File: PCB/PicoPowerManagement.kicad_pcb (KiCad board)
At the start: 4 copper layers, 138.7 x 119.1 mm, 113 parts, among them J1 UART Header, J10 GSB3CA11310DSHR, J11 GSB3CA11310DSHR, J12 GSB3CA11310DSHR, J13 GSB3CA11310DSHR, J2 DEBUG, J3 SwitchLEDS, J4 PowerSwitch, J5 NAS Fan 1, J6 NAS Fan 2, J7 ATX 24P Connection, J8 GSB3CA11310DSHR, J9 GSB3CA11310DSHR, Q1 2N3904, Q10 PMOS, Q11 PMOS, Q12 PMOS, Q13 PMOS, Q2 PMOS, Q3 PMOS, Q4 PMOS, Q5 PMOS, Q6 PMOS, Q7 PMOS, Q8 PMOS, Q9 PMOS, U10 FUSB302B10MPX, U11 FUSB302B11MPX, U12 LM338T/NOPB, U13 LM338T/NOPB, U14 LM338T/NOPB, U18 LM338T/NOPB, U19 LM338T/NOPB, U2 LP5810ADSDR, U20 LM338T/NOPB, U3 LP5810ADSDR, U4 LSF0101DRYR, U5 LSF0101DRYR, U6 FUSB002B01MPX, U7 FUSB002B10MPX, U8 FUSB002B11MPX, U9 FUSB302B01MPX

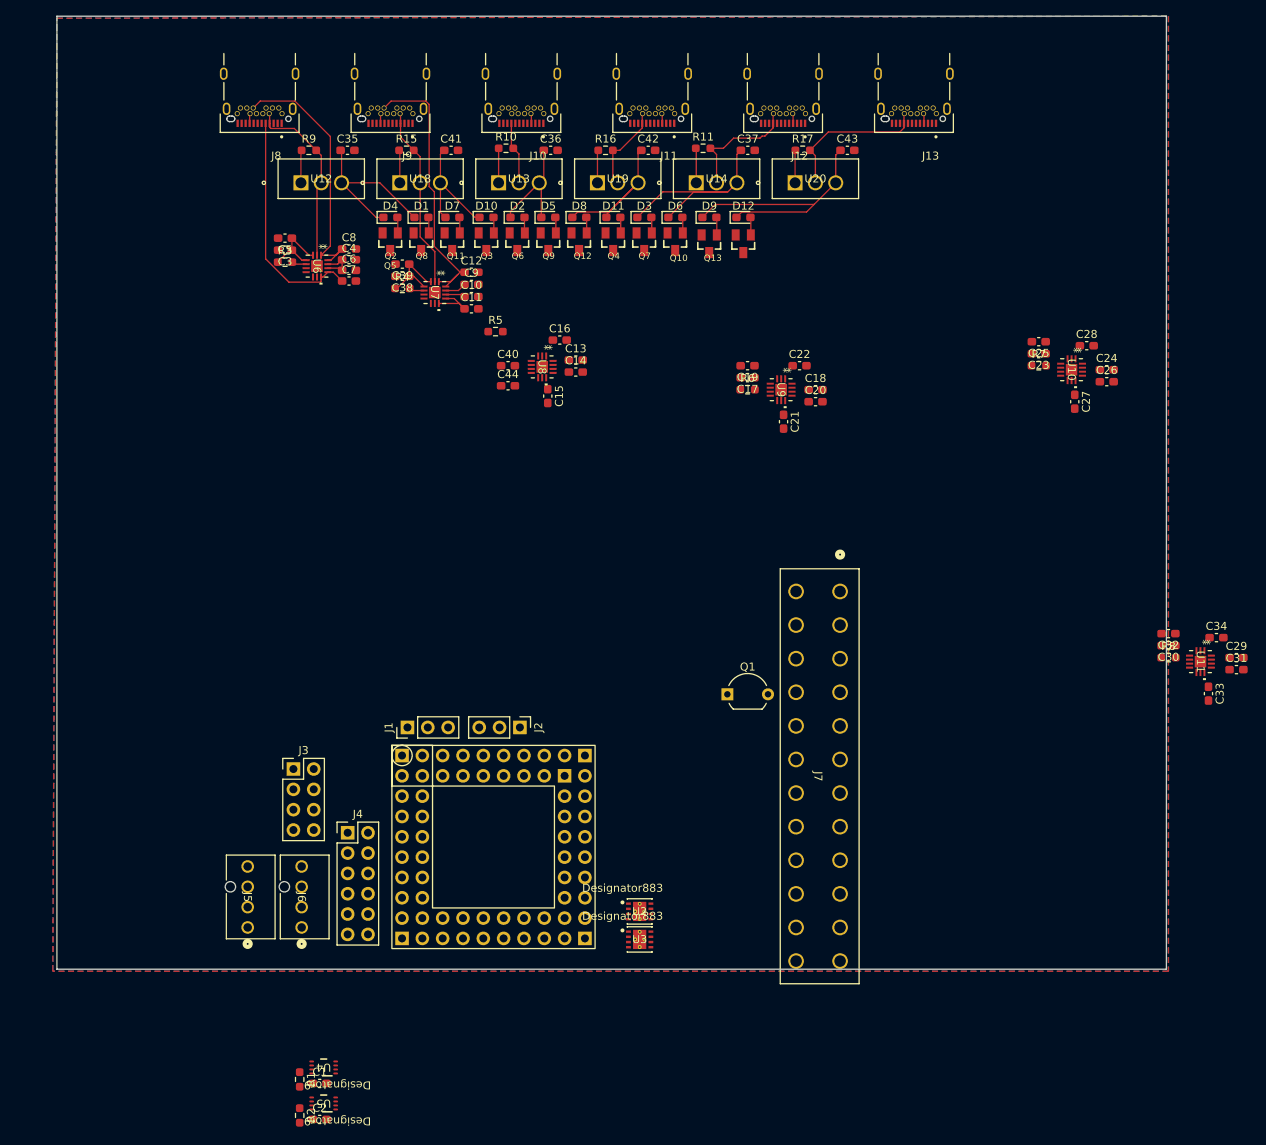
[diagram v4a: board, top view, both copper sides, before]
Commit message: Add 2N3904 component library and update footprint and symbol definitions
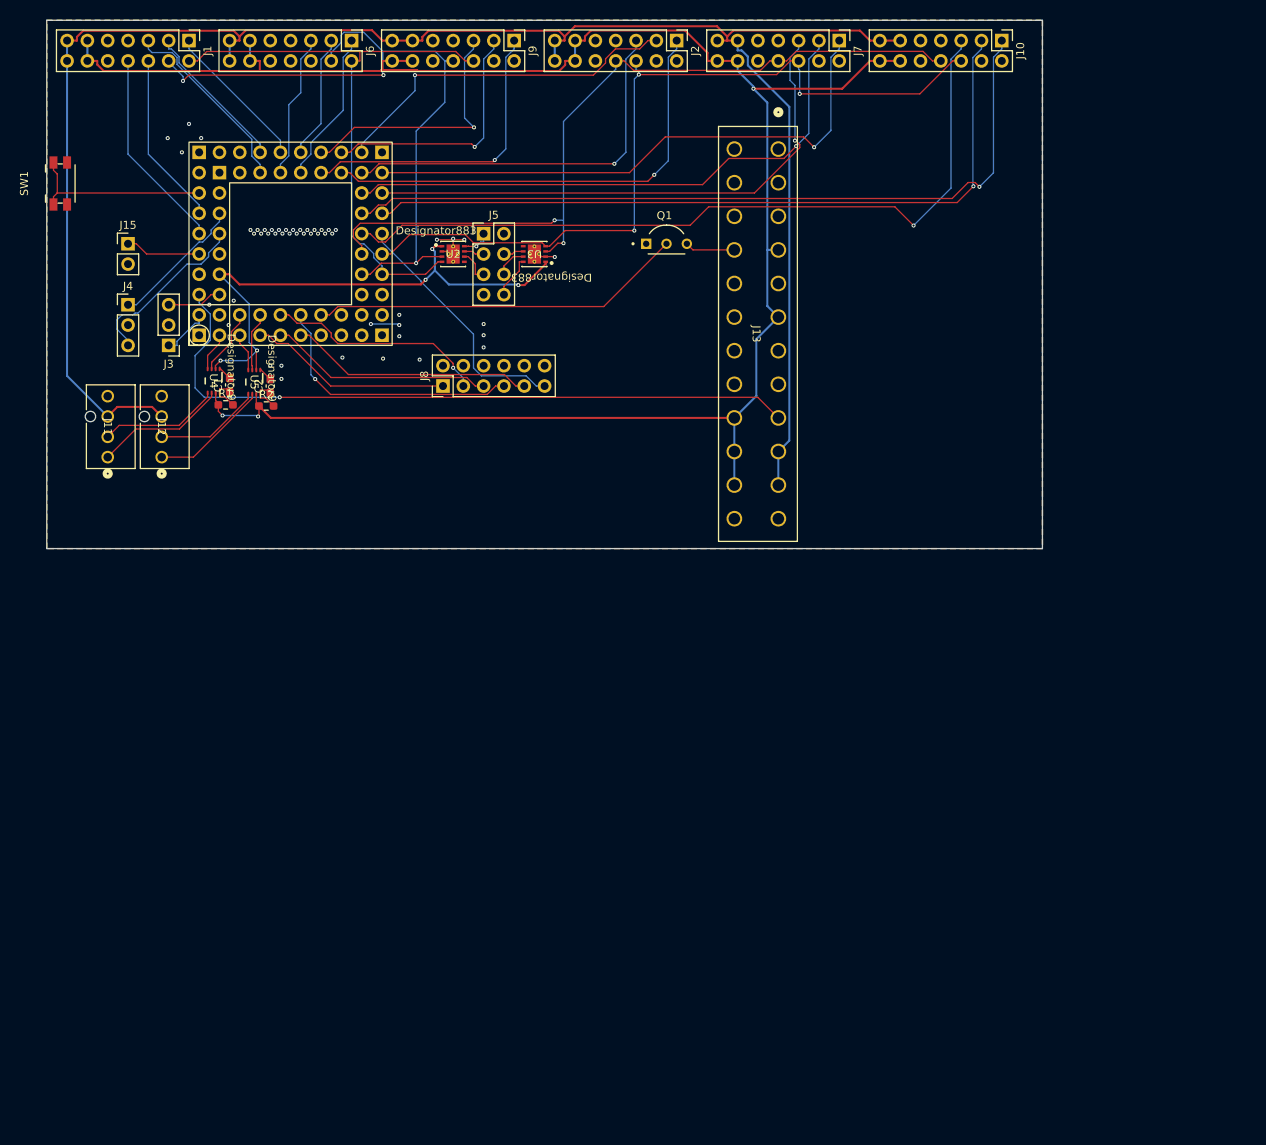
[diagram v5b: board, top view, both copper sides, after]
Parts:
- removed C10, C14, C17, C20, C23, C26, C29, C3, C32, C35, C36, C37, C38, C40, C41, C42, C43, C6: 0.1uF, Capacitor_SMD:C_0603_1608Metric_Pad1.08x0.95mm_HandSolder
- removed C11, C12, C15, C16, C21, C22, C27, C28, C33, C34, C7, C8: 200pF, Capacitor_SMD:C_0603_1608Metric_Pad1.08x0.95mm_HandSolder
- removed C13, C18, C24, C30, C4, C9: 10uF, Capacitor_SMD:C_0603_1608Metric_Pad1.08x0.95mm_HandSolder
- removed C19, C25, C31, C39, C44, C5: 1uF, Capacitor_SMD:C_0603_1608Metric_Pad1.08x0.95mm_HandSolder
- removed D1, D10, D11, D12, D2, D3, D4, D5, D6, D7, D8, D9: D_Small, Diode_SMD:D_0603_1608Metric_Pad1.05x0.95mm_HandSolder
- removed the J11 at (101.1, 32.6)
- removed the J12 at (117.4, 32.6)
- removed the J13 at (133.8, 32.6)
- removed the J8 at (52.0, 32.6)
- removed Q10, Q11, Q12, Q13, Q2, Q3, Q4, Q5, Q6, Q7, Q8, Q9: PMOS, SI2312:SOT23
- removed R10, R11, R15, R16, R17, R9: 0.25, Resistor_SMD:R_0603_1608Metric_Pad0.98x0.95mm_HandSolder
- removed R3, R4, R5, R6, R7, R8: 4.7k, Resistor_SMD:R_0603_1608Metric_Pad0.98x0.95mm_HandSolder
- removed U10: FUSB302B10MPX, FUSB302:MLP14_2P5X2P5_ONS
- removed U11: FUSB302B11MPX, FUSB302:MLP14_2P5X2P5_ONS
- removed U12, U13, U14, U18, U19, U20: LM338T/NOPB, LM338:T03B_TEX
- removed U6: FUSB002B01MPX, FUSB302:MLP14_2P5X2P5_ONS
- removed U7: FUSB002B10MPX, FUSB302:MLP14_2P5X2P5_ONS
- removed U8: FUSB002B11MPX, FUSB302:MLP14_2P5X2P5_ONS
- removed U9: FUSB302B01MPX, FUSB302:MLP14_2P5X2P5_ONS
- added J1: Conn_02x07_Odd_Even, Connector_PinHeader_2.54mm:PinHeader_2x07_P2.54mm_Vertical, F.Cu at (43.2, 22.9)
- added J15: Conn_01x02, Connector_PinHeader_2.54mm:PinHeader_1x02_P2.54mm_Vertical, F.Cu at (35.6, 48.3)
- added J2: Conn_02x07_Odd_Even, Connector_PinHeader_2.54mm:PinHeader_2x07_P2.54mm_Vertical, F.Cu at (104.1, 22.9)
- added J6: Conn_02x07_Odd_Even, Connector_PinHeader_2.54mm:PinHeader_2x07_P2.54mm_Vertical, F.Cu at (63.5, 22.9)
- added J7: Conn_02x07_Odd_Even, Connector_PinHeader_2.54mm:PinHeader_2x07_P2.54mm_Vertical, F.Cu at (124.5, 22.9)
- added SW1: SW_SPST, Button_Switch_SMD:Panasonic_EVQPUJ_EVQPUA, F.Cu at (27.1, 40.7)
- J10, J9: value GSB3CA11310DSHR -> Conn_02x07_Odd_Even; footprint GSB3CA11310DSHR:AMPHENOL_GSB3CA11310DSHR -> Connector_PinHeader_2.54mm:PinHeader_2x07_P2.54mm_Vertical
- Q1: footprint Package_TO_SOT_THT:TO-92-2_Wide -> 2N3904:TO92254P460H750-3
- moved C2 91.9 mm to (53.3, 66.0), turned to 90 degrees
- moved U5 90.6 mm to (51.3, 65.5), turned to -90 degrees
- moved R2 88.8 mm to (52.8, 68.5), turned to 0 degrees
- moved C1 88.0 mm to (48.3, 65.9), turned to 90 degrees
- moved U4 86.9 mm to (46.3, 65.4), turned to -90 degrees
- moved U3 86.7 mm to (86.4, 49.5), turned to 180 degrees
- moved U2 85.4 mm to (76.2, 49.5)
- moved R1 84.8 mm to (47.8, 68.4), turned to 0 degrees
- moved J4 72.0 mm to (35.6, 55.9), turned to 0 degrees
- moved J5 71.0 mm to (80.0, 47.0)
- moved J11 61.3 mm to (33.0, 74.9)
- moved J12 61.3 mm to (39.8, 74.9)
- moved J10 60.8 mm to (144.8, 22.9), turned to -90 degrees
- moved U1 58.3 mm to (44.5, 59.7), turned to 90 degrees
- moved J8 57.1 mm to (74.9, 66.0), turned to 90 degrees
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- renumbered J5 to J11, J6 to J12, J7 to J13, J1 to J3, J2 to J4, J3 to J5, J4 to J8
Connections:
- J13 pad 1: +3.3V -> unconnected-(J13-Pad1)
- J13 pad 12: +3.3V -> unconnected-(J13-Pad12)
- J13 pad 13: +3.3V -> unconnected-(J13-Pad13)
- J13 pad 14: -12V -> unconnected-(J13-Pad14)
- J13 pad 2: +3.3V -> unconnected-(J13-Pad2)
- J13 pad 8: /PWR_ON -> unconnected-(J13-Pad8)
- J5 pad 2: /RESET_R -> GND
- J5 pad 4: /RESET_G -> /RESET_B
- J5 pad 6: /RESET_B -> /RESET_G
- J5 pad 8: GND -> /RESET_R
- U1 pad 2: /3v3PWM1 -> /3v3RPMSignal1
- U1 pad 25: /USB0_INT -> /USB5_INT
- U1 pad 26: /USB1_INT -> /USB5_5VEN
- U1 pad 27: /USB2_INT -> /USB5_12VEN
- U1 pad 28: /USB3_INT -> /USB4_INT
- U1 pad 29: /USB4_INT -> /USB4_5VEN
- U1 pad 3: /3v3RPMSignal1 -> /3v3PWM1
- U1 pad 30: /USB5_INT -> /USB4_12VEN
- U1 pad 31: /USB0_5VEN -> /USB3_INT
- U1 pad 32: /USB1_5VEN -> /USB3_5VEN
- U1 pad 33: /USB2_5VEN -> /USB3_12VEN
- U1 pad 34: /USB3_5VEN -> /USB2_5VEN
- U1 pad 35: /USB4_5VEN -> /USB2_12VEN
- U1 pad 36: /USB5_5VEN -> /USB2_INT
- U1 pad 37: /USB0_12VEN -> /USB1_12VEN
- U1 pad 38: /USB1_12VEN -> /USB1_5VEN
- U1 pad 39: /USB2_12VEN -> /USB1_INT
- U1 pad 4: /3v3PWM2 -> /3v3RPMSignal2
- U1 pad 40: /USB3_12VEN -> /USB0_12VEN
- U1 pad 41: /USB4_12VEN -> /USB0_INT
- U1 pad 42: /USB5_12VEN -> /USB0_5VEN
- U1 pad 5: /3v3RPMSignal2 -> /3v3PWM2
- U2 pad 10: (no net) -> GND
- U2 pad 11: (no net) -> GND
- U2 pad 12: (no net) -> GND
- U2 pad 13: (no net) -> GND
- U2 pad 9: unconnected-(U2-GND-Pad9) -> GND
- U3 pad 10: (no net) -> GND
- U3 pad 11: (no net) -> GND
- U3 pad 12: (no net) -> GND
- U3 pad 13: (no net) -> GND
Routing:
- net +5V: track 0.00 -> 250.7 mm, vias 0 -> 3
- net +12V: track 0.00 -> 236.6 mm
- net SDA1: track 0.00 -> 102.3 mm, vias 0 -> 3
- net SCL1: track 0.00 -> 100.9 mm, vias 0 -> 2
- net /USB5_12VEN: track 0.00 -> 98.5 mm, vias 0 -> 1
- net /USB5_INT: track 0.00 -> 97.8 mm, vias 0 -> 1
- net /USB5_5VEN: track 0.00 -> 94.0 mm, vias 0 -> 1
- net SCL0: track 0.00 -> 88.7 mm, vias 0 -> 3
- net /+5VDC_Standby: track 0.00 -> 87.5 mm, vias 0 -> 1
- net SDA0: track 0.00 -> 75.4 mm
- net /USB4_5VEN: track 0.00 -> 71.1 mm, vias 0 -> 1
- net /USB4_12VEN: track 0.00 -> 71.0 mm, vias 0 -> 1
- net /USB4_INT: track 0.00 -> 69.0 mm, vias 0 -> 1
- net /USB3_12VEN: track 0.00 -> 57.8 mm, vias 0 -> 1
- net /USB3_INT: track 0.00 -> 48.6 mm, vias 0 -> 1
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- removed copper zone on In1.Cu, net GND
- removed copper zone on In2.Cu, net GND
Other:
- board size 138.7 x 119.1 mm -> 124.5 x 66 mm
- copper layers 4 -> 2

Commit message: confused now
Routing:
- net +12V: track 236.6 -> 294.5 mm, vias 0 -> 8
- net GND: track 22.4 -> 0.00 mm, vias 49 -> 0
- net +5V: track 250.7 -> 264.8 mm, vias 3 -> 5
- net /USB3_5VEN: track 44.7 -> 52.9 mm, vias 1 -> 2
- net /PWR: track 31.3 -> 38.1 mm, vias 0 -> 1
- net SDA0: track 75.4 -> 81.4 mm, vias 0 -> 3
- net SCL1: track 100.9 -> 106.7 mm, vias 2 -> 4
- net /USB0_INT: track 23.8 -> 28.0 mm, vias 0 -> 1
- net /PSU_ON: track 46.9 -> 51.0 mm, vias 0 -> 1
- net /SWDIO: track 17.0 -> 21.0 mm, vias 0 -> 1
- net /USB0_5VEN: track 18.9 -> 22.8 mm, vias 0 -> 1
- net /USB0_12VEN: track 18.7 -> 22.6 mm, vias 0 -> 1
- net /+5VDC_Standby: track 87.5 -> 84.0 mm, vias 1 -> 2
- net /USB3_12VEN: track 57.8 -> 54.4 mm, vias 1 -> 3
- net SDA1: track 102.3 -> 105.5 mm, vias 3 -> 8
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
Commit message: confused now
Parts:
- moved J10 117.5 mm to (43.2, 81.9)
- moved J7 85.0 mm to (63.5, 82.0)
- moved J2 62.6 mm to (83.8, 82.0)
- moved Q1 27.4 mm to (76.3, 41.7)
- moved J13 23.4 mm to (94.3, 30.4)
- moved J8 16.8 mm to (59.3, 72.3)
- moved J9 15.5 mm to (68.6, 25.4), turned to 90 degrees
- moved J6 15.5 mm to (48.3, 25.4), turned to 90 degrees
- moved J1 15.3 mm to (28.1, 25.4), turned to 90 degrees
- moved J5 3.19 mm to (76.8, 46.6)
- moved U2 3.19 mm to (73.0, 49.1)
- moved U3 3.19 mm to (83.2, 49.1)
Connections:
- J1 pad 1: /USB0_12VEN -> +5V
- J1 pad 10: GND -> SDA0
- J1 pad 11: +5V -> /USBD+
- J1 pad 12: +5V -> SCL0
- J1 pad 13: +12V -> /USBD-
- J1 pad 14: +12V -> +3.3V
- J1 pad 2: SDA0 -> +12V
- J1 pad 3: /USB0_5VEN -> +5V
- J1 pad 4: SCL0 -> +12V
- J1 pad 5: /USB0_INT -> GND
- J1 pad 6: /USBD- -> GND
- J1 pad 7: GND -> /USB0_5VEN
- J1 pad 8: /USBD+ -> /USB0_12VEN
- J1 pad 9: GND -> /USB0_INT
- J10 pad 1: /USB5_12VEN -> +12V
- J10 pad 10: GND -> SDA1
- J10 pad 11: +12V -> unconnected-(J10-Pin_11-Pad11)
- J10 pad 12: +5V -> SCL1
- J10 pad 13: +12V -> unconnected-(J10-Pin_13-Pad13)
- J10 pad 14: +5V -> +3.3V
- J10 pad 2: unconnected-(J10-Pin_2-Pad2) -> +5V
- J10 pad 3: /USB5_5VEN -> +12V
- J10 pad 4: unconnected-(J10-Pin_4-Pad4) -> +5V
- J10 pad 5: /USB5_INT -> GND
- J10 pad 6: SDA1 -> GND
- J10 pad 7: GND -> /USB5_5VEN
- J10 pad 8: SCL1 -> /USB5_12VEN
- J10 pad 9: GND -> /USB5_INT
- J2 pad 1: /USB3_12VEN -> +12V
- J2 pad 10: GND -> SDA1
- J2 pad 11: +5V -> unconnected-(J2-Pin_11-Pad11)
- J2 pad 12: +5V -> SCL1
- J2 pad 13: +12V -> unconnected-(J2-Pin_13-Pad13)
- J2 pad 14: +12V -> +3.3V
- J2 pad 2: unconnected-(J2-Pin_2-Pad2) -> +5V
- J2 pad 3: /USB3_5VEN -> +12V
- J2 pad 4: unconnected-(J2-Pin_4-Pad4) -> +5V
- J2 pad 5: /USB3_INT -> GND
- J2 pad 6: SDA1 -> GND
- J2 pad 7: GND -> /USB3_5VEN
- J2 pad 8: SCL1 -> /USB3_12VEN
- J2 pad 9: GND -> /USB3_INT
- J6 pad 1: /USB1_12VEN -> +12V
- J6 pad 10: GND -> SDA0
- J6 pad 11: +5V -> unconnected-(J6-Pin_11-Pad11)
- J6 pad 12: +5V -> SCL0
- J6 pad 13: +12V -> unconnected-(J6-Pin_13-Pad13)
- J6 pad 14: +12V -> +3.3V
- J6 pad 2: SDA0 -> +5V
- J6 pad 3: /USB1_5VEN -> +12V
- J6 pad 4: SCL0 -> +5V
- J6 pad 5: /USB1_INT -> GND
- J6 pad 6: unconnected-(J6-Pin_6-Pad6) -> GND
- J6 pad 7: GND -> /USB1_5VEN
- J6 pad 8: unconnected-(J6-Pin_8-Pad8) -> /USB1_12VEN
- J6 pad 9: GND -> /USB1_INT
- J7 pad 1: /USB4_12VEN -> +12V
- J7 pad 10: GND -> SDA1
- J7 pad 11: +12V -> unconnected-(J7-Pin_11-Pad11)
- J7 pad 12: +5V -> SCL1
- J7 pad 13: +12V -> unconnected-(J7-Pin_13-Pad13)
- J7 pad 14: +5V -> +3.3V
- J7 pad 2: unconnected-(J7-Pin_2-Pad2) -> +5V
- J7 pad 3: /USB4_5VEN -> +12V
- J7 pad 4: unconnected-(J7-Pin_4-Pad4) -> +5V
- J7 pad 5: /USB4_INT -> GND
- J7 pad 6: SDA1 -> GND
- J7 pad 7: GND -> /USB4_5VEN
- J7 pad 8: SCL1 -> /USB4_12VEN
- J7 pad 9: GND -> /USB4_INT
- J9 pad 1: /USB2_12VEN -> +12V
- J9 pad 10: GND -> SDA0
- J9 pad 11: +12V -> unconnected-(J9-Pin_11-Pad11)
- J9 pad 12: +5V -> SCL0
- J9 pad 13: +12V -> unconnected-(J9-Pin_13-Pad13)
- J9 pad 14: +5V -> +3.3V
- J9 pad 2: unconnected-(J9-Pin_2-Pad2) -> +5V
- J9 pad 3: /USB2_5VEN -> +12V
- J9 pad 4: unconnected-(J9-Pin_4-Pad4) -> +5V
- J9 pad 5: /USB2_INT -> GND
- J9 pad 6: SDA0 -> GND
- J9 pad 7: GND -> /USB2_5VEN
- J9 pad 8: SCL0 -> /USB2_12VEN
- J9 pad 9: GND -> /USB2_INT
- U2 pad 10: GND -> (no net)
- U2 pad 11: GND -> (no net)
- U2 pad 12: GND -> (no net)
- U2 pad 13: GND -> (no net)
- U3 pad 10: GND -> (no net)
- U3 pad 11: GND -> (no net)
- U3 pad 12: GND -> (no net)
- U3 pad 13: GND -> (no net)
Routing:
- net +3.3V: track 65.5 -> 208.1 mm
- net +12V: track 294.5 -> 177.4 mm, vias 8 -> 1
- net +5V: track 264.8 -> 227.2 mm, vias 5 -> 4
- net /USB5_12VEN: track 99.4 -> 64.6 mm
- net /USB5_INT: track 95.7 -> 63.3 mm, vias 2 -> 1
- net /USB5_5VEN: track 93.6 -> 65.6 mm
- net /+5VDC_Standby: track 84.0 -> 56.3 mm, vias 2 -> 1
- net /USB4_5VEN: track 71.7 -> 48.3 mm
- net /PSU_ON: track 51.0 -> 31.4 mm
- net /USB4_INT: track 68.7 -> 53.5 mm
- net /USB4_12VEN: track 69.3 -> 56.9 mm, vias 1 -> 2
- net /PWR: track 38.1 -> 27.2 mm, vias 1 -> 0
- net /Pi2_On: track 30.0 -> 20.0 mm
- net /Pi4_On: track 32.3 -> 22.8 mm
- net /USB2_5VEN: track 32.2 -> 23.3 mm
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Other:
- board size 124.5 x 66 mm -> 71.2 x 66 mm
- board text added: "+12V"
- board text added: "B"
- board text added: "Display"
- board text added: "G"
- board text added: "GND"
- board text added: "PWM"
- board text added: "Pi1"
- board text added: "Pi2"
- board text added: "Pi3"
- board text added: "Pi4"
- board text added: "Power"
- board text added: "R"
- board text added: "RESET"
- board text added: "RPM"
- board text added: "RX"
- board text added: "Reset"
- board text added: "SWCLK"
- board text added: "SWDIO"
- board text added: "TX"

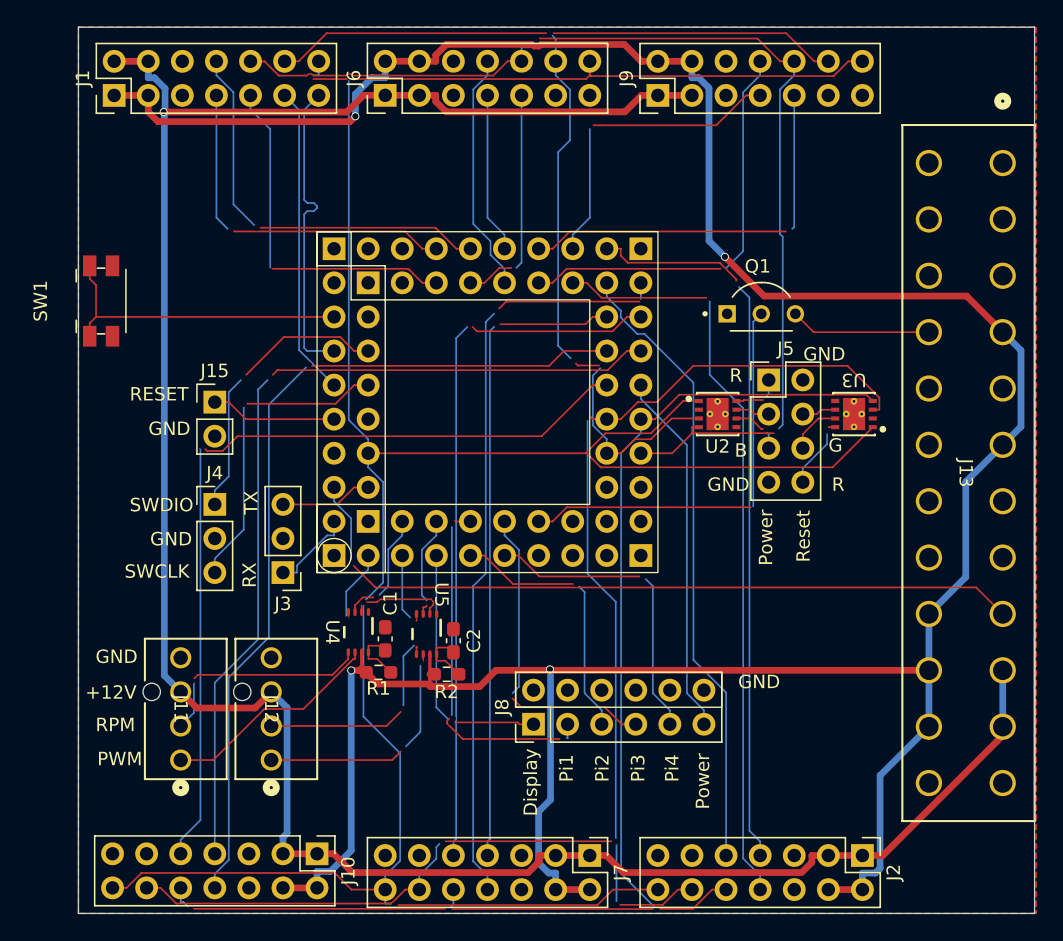
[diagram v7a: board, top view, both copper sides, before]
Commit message: updating rules and fixing footprints
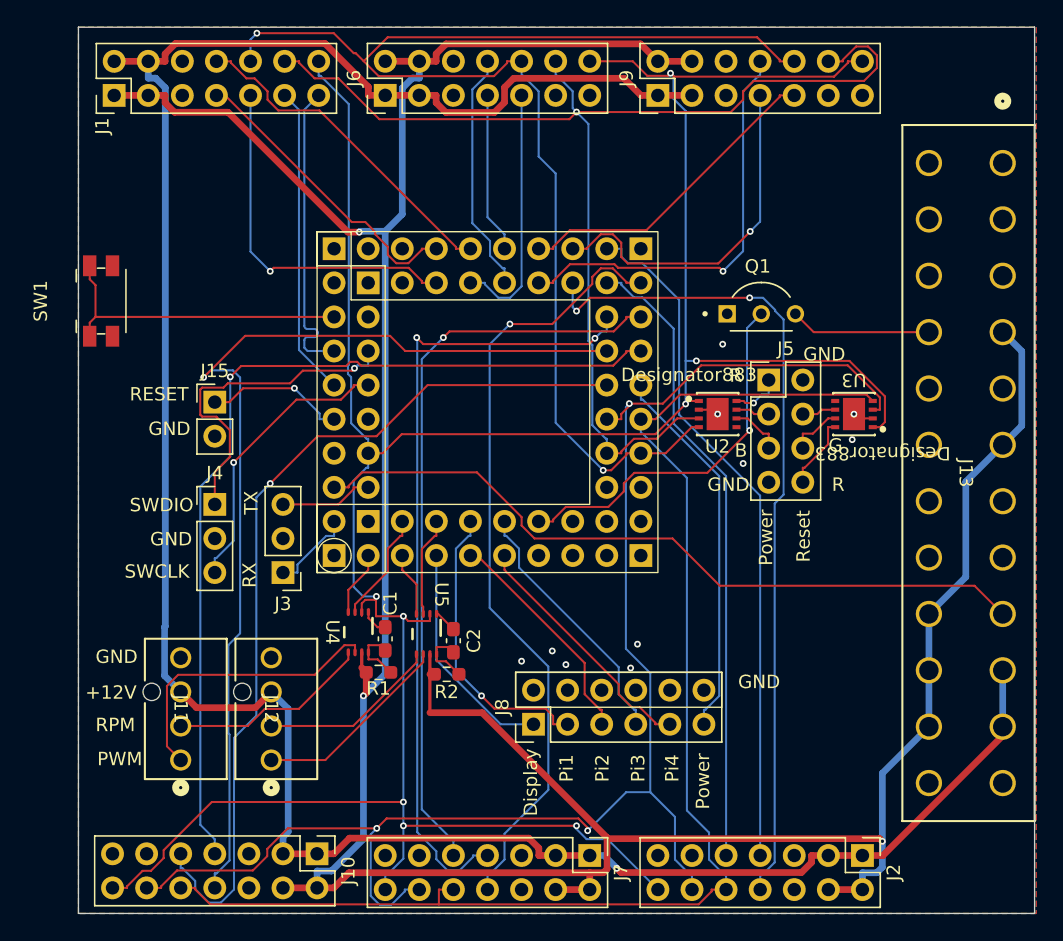
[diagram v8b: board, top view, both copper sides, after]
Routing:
- net SDA0: track 83.6 -> 99.1 mm
- net +5V: track 227.2 -> 241.6 mm, vias 4 -> 3
- net /USB4_5VEN: track 48.3 -> 60.0 mm, vias 1 -> 2
- net /USB5_12VEN: track 64.6 -> 73.9 mm
- net SCL1: track 107.6 -> 114.7 mm, vias 4 -> 3
- net GND: track 0.00 -> 6.78 mm, vias 14 -> 10
- net SCL0: track 85.7 -> 92.2 mm, vias 3 -> 1
- net /USB3_12VEN: track 56.3 -> 62.1 mm, vias 1 -> 2
- net /USB2_INT: track 29.5 -> 23.9 mm, vias 1 -> 0
- net +12V: track 177.4 -> 182.8 mm
- net /Pi1_On: track 27.2 -> 22.0 mm, vias 3 -> 1
- net /5V PWM1: track 16.6 -> 21.7 mm
- net /USB0_12VEN: track 30.2 -> 25.2 mm, vias 1 -> 0
- net /Pi3_On: track 24.0 -> 19.3 mm, vias 1 -> 0
- net /Pi4_On: track 22.8 -> 18.7 mm, vias 1 -> 0
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- added copper zone on In1.Cu, net GND
- added copper zone on In2.Cu, net GND
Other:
- copper layers 2 -> 4
